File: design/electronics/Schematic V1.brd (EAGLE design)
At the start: 152.4 x 139.7 mm, 205 parts, among them J1 PJ-202AH, J2 TSM-103-01-L-SVJ, J3 DD50P564GTXLF, J4 DD50P564GTXLF, J5 TSM-103-01-L-SVJ

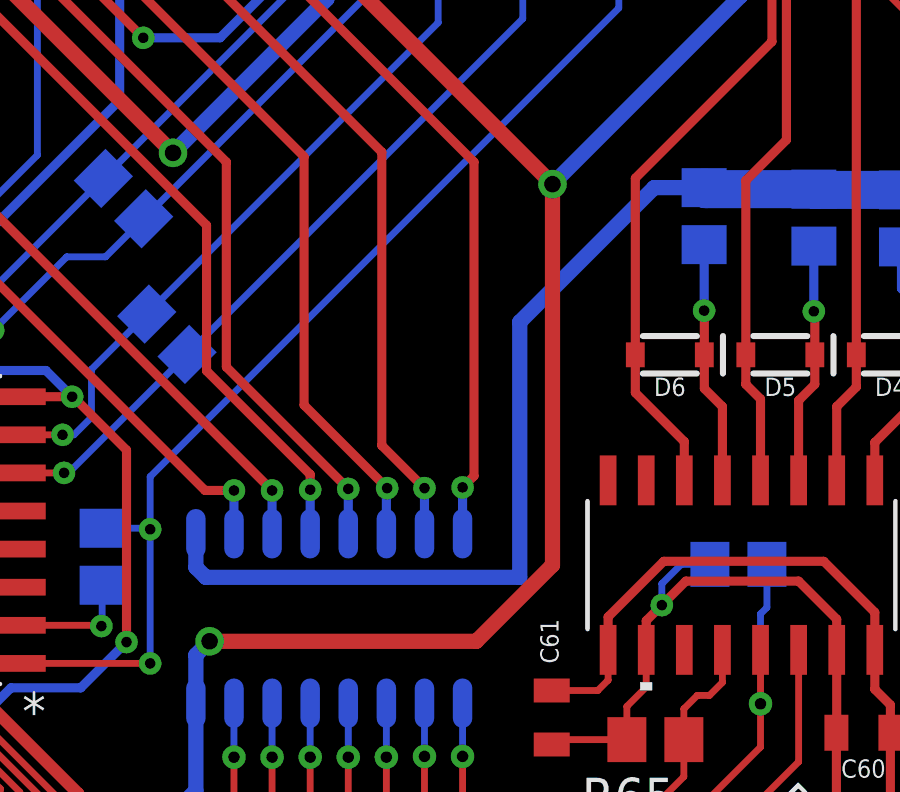
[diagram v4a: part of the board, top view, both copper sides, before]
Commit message: Updated silkscreen and trace error
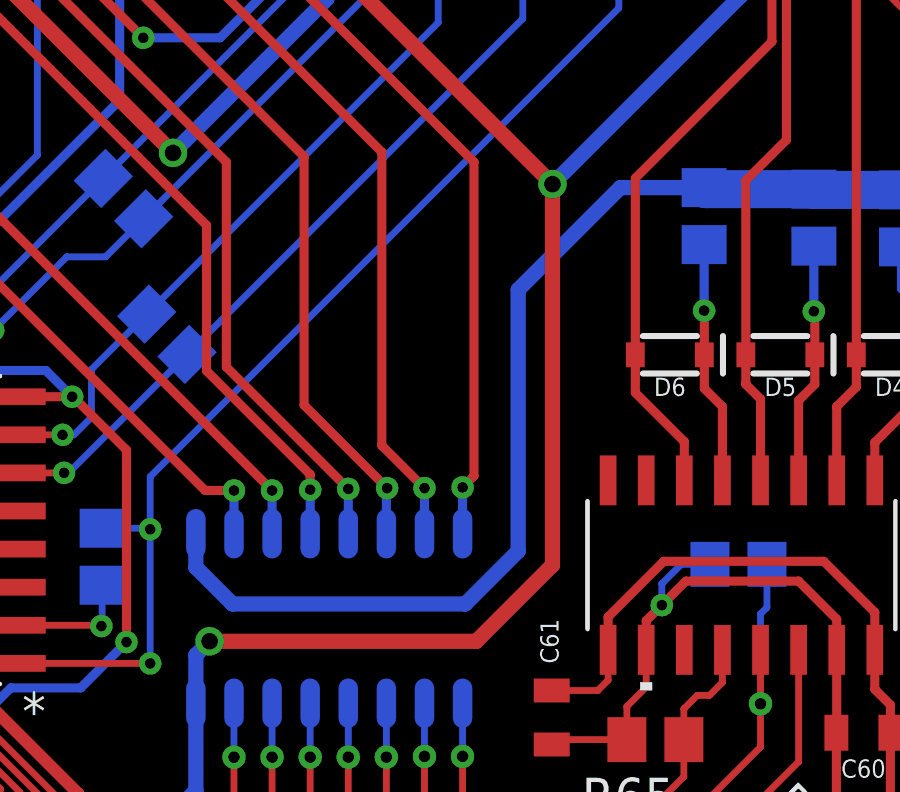
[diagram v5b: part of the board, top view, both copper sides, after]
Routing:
- net +24V: track 446.8 -> 447.6 mm
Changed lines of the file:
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@@
 <wire x1="114.1222" y1="116.6724" x2="110.5154" y2="116.6724" width="1.27" layer="16"/>
 <wire x1="110.5154" y1="116.6724" x2="110.4646" y2="116.7232" width="1.27" layer="16"/>
-<wire x1="110.4646" y1="116.7232" x2="108.7984" y2="116.7232" width="0.508" layer="16"/>
-<wire x1="104.3178" y1="112.2426" x2="104.3178" y2="103.7336" width="0.508" layer="16"/>
+<wire x1="110.4646" y1="116.7232" x2="107.6706" y2="116.7232" width="0.508" layer="16"/>
+<wire x1="107.6706" y1="116.7232" x2="104.267" y2="113.3196" width="0.508" layer="16"/>
+<wire x1="104.267" y1="113.3196" x2="104.267" y2="104.6074" width="0.508" layer="16"/>
+<wire x1="104.267" y1="104.6074" x2="102.5042" y2="102.8446" width="0.508" layer="16"/>
 <wire x1="93.5228" y1="104.0638" x2="93.5228" y2="105.186996875" width="0.508" layer="16"/>
-<wire x1="108.7984" y1="116.7232" x2="104.3178" y2="112.2426" width="0.508" layer="16"/>
-<wire x1="104.3178" y1="103.7336" x2="93.853" y2="103.7336" width="0.508" layer="16"/>
-<wire x1="93.853" y1="103.7336" x2="93.5228" y2="104.0638" width="0.508" layer="16"/>
+<wire x1="102.5042" y1="102.8446" x2="94.742" y2="102.8446" width="0.508" layer="16"/>
+<wire x1="94.742" y1="102.8446" x2="93.5228" y2="104.0638" width="0.508" layer="16"/>
 <via x="146.8628" y="116.6114" extent="1-16" drill="1.27"/>
 <wire x1="146.8272" y1="116.647" x2="146.8628" y2="116.6114" width="1.27" layer="16"/>
